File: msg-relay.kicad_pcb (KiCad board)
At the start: 2 copper layers, 100 x 100 mm, 6 parts, among them J1 Screw_Terminal_01x02, K1 SANYOU_SRD_Form_C, K2 SANYOU_SRD_Form_C, K3 SANYOU_SRD_Form_C, K4 SANYOU_SRD_Form_C

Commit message: Some work on schema
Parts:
- added D1: 1N4007, Diode_THT:D_DO-41_SOD81_P10.16mm_Horizontal, F.Cu at (146.9, 55.5)
- added D2: 1N4007, Diode_THT:D_DO-41_SOD81_P10.16mm_Horizontal, F.Cu at (147.4, 81.2)
- added D3: 1N4007, Diode_THT:D_DO-41_SOD81_P10.16mm_Horizontal, F.Cu at (144.6, 100.5)
- added D4: 1N4007, Diode_THT:D_DO-41_SOD81_P10.16mm_Horizontal, F.Cu at (149.1, 121.7)
- added J2: Conn_01x03_Male, Connector_Phoenix_MC_HighVoltage:PhoenixContact_MCV_1,5_3-G-5.08_1x03_P5.08mm_Vertical, F.Cu at (175.1, 55.7)
- added J3: Conn_01x03_Male, Connector_Phoenix_MC_HighVoltage:PhoenixContact_MCV_1,5_3-G-5.08_1x03_P5.08mm_Vertical, F.Cu at (175.5, 81.8)
- added J4: Conn_01x03_Male, Connector_Phoenix_MC_HighVoltage:PhoenixContact_MCV_1,5_3-G-5.08_1x03_P5.08mm_Vertical, F.Cu at (174.6, 101.3)
- added J5: Conn_01x03_Male, Connector_Phoenix_MC_HighVoltage:PhoenixContact_MCV_1,5_3-G-5.08_1x03_P5.08mm_Vertical, F.Cu at (176.4, 122.6)
- added Q1: BC847, Package_TO_SOT_SMD:SOT-23, F.Cu at (141.7, 65.5)
- added Q2: BC847, Package_TO_SOT_SMD:SOT-23, F.Cu at (141.8, 91.4)
- added Q3: BC847, Package_TO_SOT_SMD:SOT-23, F.Cu at (140.1, 110.7)
- added Q4: BC847, Package_TO_SOT_SMD:SOT-23, F.Cu at (144.3, 131.9)
- added R1: R, Resistor_SMD:R_0603_1608Metric, F.Cu at (142.2, 60.4)
- added R2: R, Resistor_SMD:R_0603_1608Metric, F.Cu at (142.7, 84.7)
- added R3: R, Resistor_SMD:R_0603_1608Metric, F.Cu at (141.2, 104.6)
- added R4: R, Resistor_SMD:R_0603_1608Metric, F.Cu at (143.4, 125.0)
- moved J1 81.2 mm to (115.2, 55.0)
- moved A1 36.5 mm to (125.7, 67.0), turned to 270 degrees
- moved K3 27.0 mm to (149.2, 106.3)
- moved K2 16.4 mm to (151.9, 87.0)
- moved K4 16.3 mm to (153.5, 127.6)
- moved K1 10.5 mm to (152.1, 61.1)
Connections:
- A1 pad 11: Net-(A1-Pad11) -> RELAY1
- A1 pad 12: Net-(A1-Pad12) -> RELAY2
- A1 pad 13: Net-(A1-Pad13) -> RELAY3
- A1 pad 14: Net-(A1-Pad14) -> RELAY4
- A1 pad 27: Net-(A1-Pad27) -> +5V
- A1 pad 29: Net-(A1-Pad29) -> GND
- A1 pad 30: Net-(A1-Pad30) -> +12V
- A1 pad 4: Net-(A1-Pad4) -> GND
- J1 pad 1: Net-(J1-Pad1) -> GND
- J1 pad 2: Net-(J1-Pad2) -> +12V
- K1 pad 5: Net-(K1-Pad5) -> +5V
- K2 pad 5: Net-(K2-Pad5) -> +5V
- K3 pad 5: Net-(K3-Pad5) -> +5V
- K4 pad 5: Net-(K4-Pad5) -> +5V
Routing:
- net Net-(J2-Pad2): track 0.00 -> 23.1 mm
- net Net-(D1-Pad2): track 0.00 -> 12.0 mm
- net Net-(J2-Pad3): track 0.00 -> 10.0 mm
- net Net-(J2-Pad1): track 0.00 -> 9.06 mm
- net +5V: track 0.00 -> 7.31 mm
- net Net-(Q1-Pad1): track 0.00 -> 4.00 mm

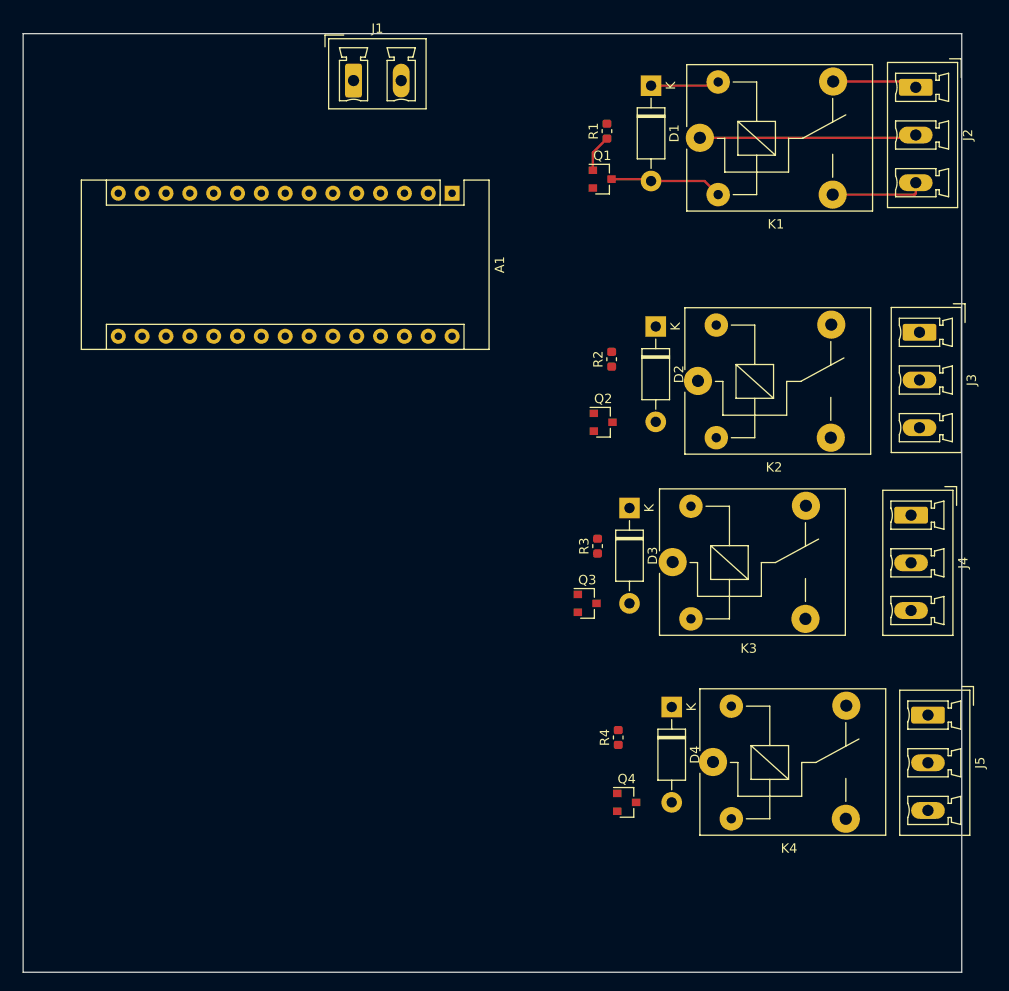
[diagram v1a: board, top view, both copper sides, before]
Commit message: Split out relay to own schema
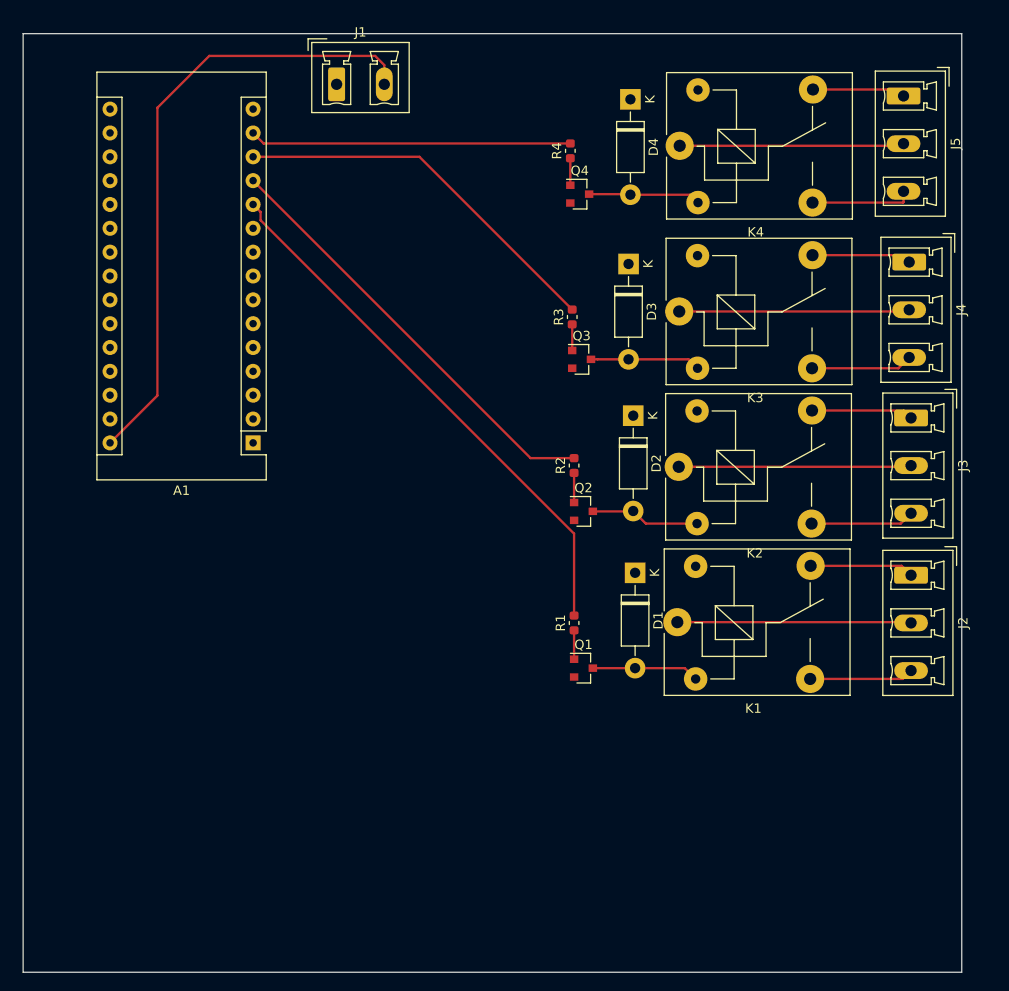
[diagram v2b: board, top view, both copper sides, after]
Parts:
- moved J5 66.0 mm to (173.8, 56.6)
- moved K4 65.7 mm to (149.9, 62.0)
- moved Q4 65.0 mm to (139.3, 67.1)
- moved D4 64.9 mm to (144.7, 57.0)
- moved R4 62.7 mm to (138.3, 62.5)
- moved R1 52.5 mm to (138.7, 112.8)
- moved Q1 52.1 mm to (139.7, 117.6)
- moved J2 52.0 mm to (174.6, 107.7)
- moved D1 51.9 mm to (145.2, 107.4)
- moved K1 51.7 mm to (149.7, 112.7)
- moved A1 34.0 mm to (104.5, 93.6), turned to 180 degrees
- moved J4 27.0 mm to (174.4, 74.3)
- moved K3 26.7 mm to (149.9, 79.6)
- moved Q3 26.0 mm to (139.5, 84.7)
- moved D3 26.0 mm to (144.5, 74.5)
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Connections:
- R2 pad 2: RELAY3 -> RELAY2
- R3 pad 2: RELAY4 -> RELAY3
- R4 pad 2: RELAY2 -> RELAY4
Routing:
- net +12V: track 0.00 -> 66.7 mm
- net RELAY1: track 0.00 -> 58.0 mm
- net RELAY2: track 0.00 -> 46.4 mm
- net RELAY3: track 0.00 -> 40.7 mm
- net RELAY4: track 0.00 -> 34.3 mm
- net Net-(J3-Pad2): track 0.00 -> 24.8 mm
- net Net-(J4-Pad2): track 0.00 -> 24.6 mm
- net Net-(J5-Pad2): track 0.00 -> 23.9 mm
- net Net-(D4-Pad2): track 0.00 -> 12.0 mm
- net Net-(D3-Pad2): track 0.00 -> 11.7 mm
- net Net-(D2-Pad2): track 0.00 -> 11.7 mm
- net Net-(J3-Pad3): track 0.00 -> 11.1 mm
- net Net-(J3-Pad1): track 0.00 -> 10.9 mm
- net Net-(J5-Pad3): track 0.00 -> 10.9 mm
- net Net-(J4-Pad3): track 0.00 -> 10.8 mm
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
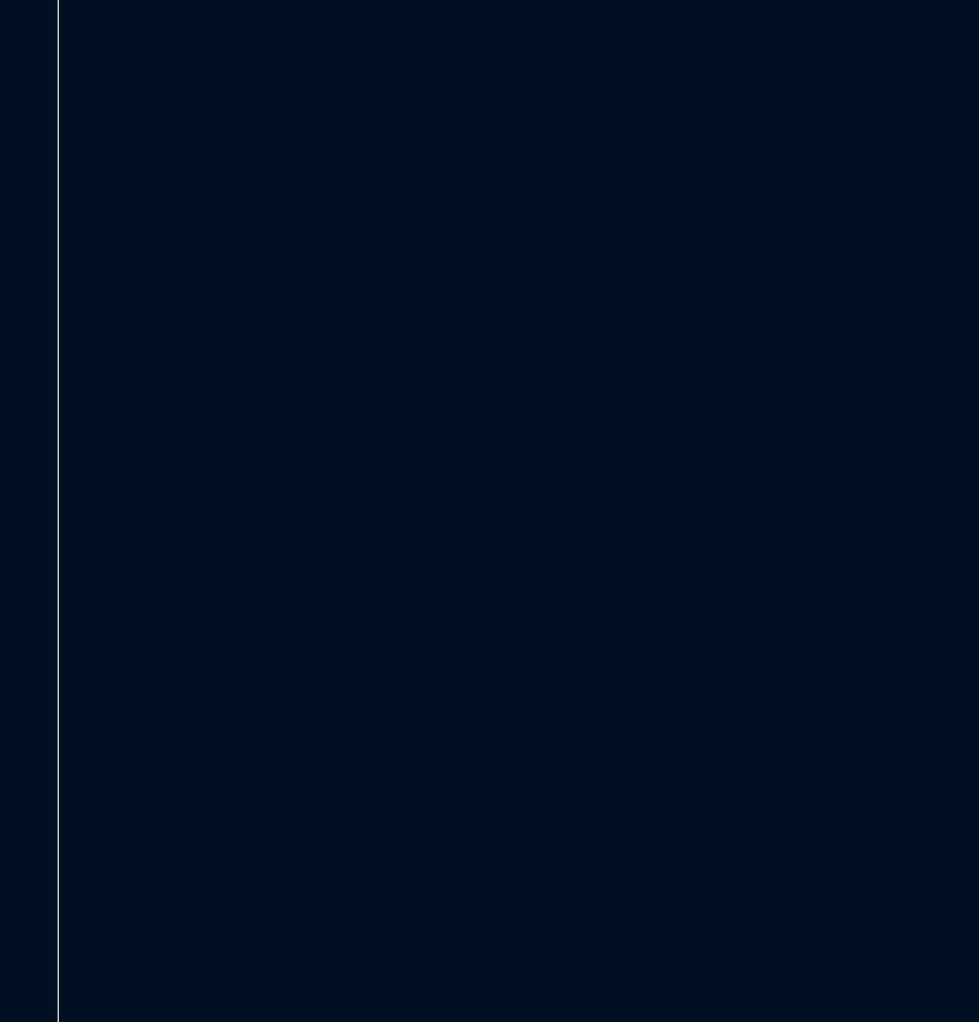
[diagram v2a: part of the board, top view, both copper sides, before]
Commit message: Added input module
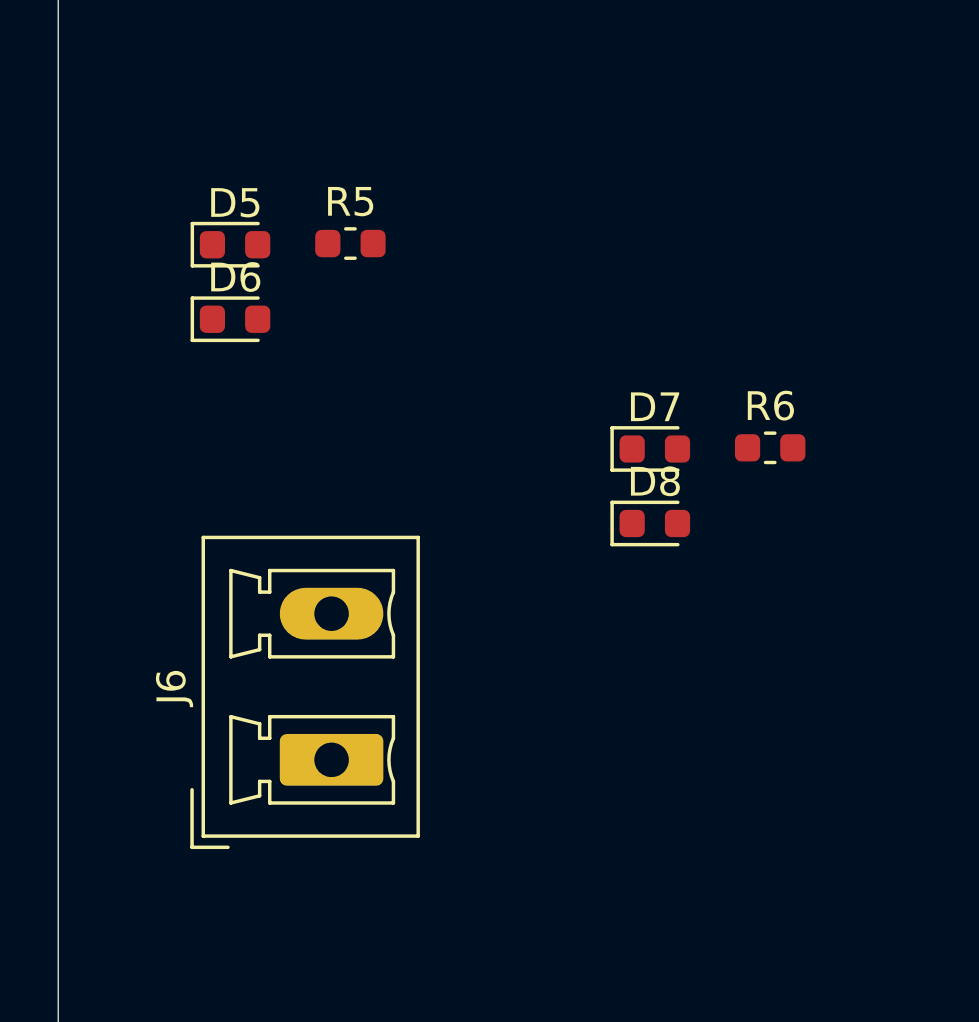
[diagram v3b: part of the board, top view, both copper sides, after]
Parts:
- added D5: D, Diode_SMD:D_0603_1608Metric, F.Cu at (86.1, 119.7)
- added D6: D, Diode_SMD:D_0603_1608Metric, F.Cu at (86.1, 122.3)
- added D7: D, Diode_SMD:D_0603_1608Metric, F.Cu at (100.7, 126.8)
- added D8: D, Diode_SMD:D_0603_1608Metric, F.Cu at (100.7, 129.4)
- added J6: Screw_Terminal_01x02, Connector_Phoenix_MC_HighVoltage:PhoenixContact_MCV_1,5_2-G-5.08_1x02_P5.08mm_Vertical, F.Cu at (89.5, 137.6)
- added R5: R, Resistor_SMD:R_0603_1608Metric, F.Cu at (90.2, 119.7)
- added R6: R, Resistor_SMD:R_0603_1608Metric, F.Cu at (104.7, 126.8)
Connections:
- A1 pad 5: Net-(A1-Pad5) -> /Input1/OUT
- A1 pad 6: Net-(A1-Pad6) -> /Input2/OUT

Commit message: Made v01
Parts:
- added D10: BAT43, Diode_THT:D_DO-35_SOD27_P7.62mm_Horizontal, F.Cu at (91.8, 123.0)
- added D11: BAT43, Diode_THT:D_DO-35_SOD27_P7.62mm_Horizontal, F.Cu at (101.2, 115.5)
- added D12: BAT43, Diode_THT:D_DO-35_SOD27_P7.62mm_Horizontal, F.Cu at (96.8, 123.0)
- added D9: BAT43, Diode_THT:D_DO-35_SOD27_P7.62mm_Horizontal, F.Cu at (87.2, 115.4)
- added J7: Conn_01x03_Male, Connector_Phoenix_MC_HighVoltage:PhoenixContact_MCV_1,5_3-G-5.08_1x03_P5.08mm_Vertical, F.Cu at (152.0, 111.0)
- added R10: 10k, Resistor_SMD:R_0603_1608Metric, F.Cu at (82.0, 122.2)
- added R11: 10k, Resistor_SMD:R_0603_1608Metric, F.Cu at (96.8, 127.2)
- added R12: 10k, Resistor_SMD:R_0603_1608Metric, F.Cu at (106.2, 122.3)
- added R7: 1k, Resistor_SMD:R_0603_1608Metric, F.Cu at (119.8, 111.0)
- added R8: 10k, Resistor_SMD:R_0603_1608Metric, F.Cu at (117.8, 122.0)
- added R9: 10k, Resistor_SMD:R_0603_1608Metric, F.Cu at (91.8, 127.5)
- D1, D3: value 1N4007 -> LED; footprint Diode_THT:D_DO-41_SOD81_P10.16mm_Horizontal -> LED_SMD:LED_0603_1608Metric
- D2, D4: value 1N4007 -> 1N4148; footprint Diode_THT:D_DO-41_SOD81_P10.16mm_Horizontal -> Diode_THT:D_DO-35_SOD27_P7.62mm_Horizontal
- D5, D7: value D -> LED; footprint Diode_SMD:D_0603_1608Metric -> LED_SMD:LED_0603_1608Metric
- D6, D8: value D -> 1N4148; footprint Diode_SMD:D_0603_1608Metric -> Diode_THT:D_DO-35_SOD27_P7.62mm_Horizontal
- J2: value Conn_01x03_Male -> Screw_Terminal_01x02; footprint Connector_Phoenix_MC_HighVoltage:PhoenixContact_MCV_1,5_3-G-5.08_1x03_P5.08mm_Vertical -> Connector_Phoenix_MC_HighVoltage:PhoenixContact_MCV_1,5_2-G-5.08_1x02_P5.08mm_Vertical
- J3: value Conn_01x03_Male -> Conn_01x04; footprint Connector_Phoenix_MC_HighVoltage:PhoenixContact_MCV_1,5_3-G-5.08_1x03_P5.08mm_Vertical -> Connector_PinSocket_1.27mm:PinSocket_1x04_P1.27mm_Vertical
- J6: value Screw_Terminal_01x02 -> Conn_01x03_Male; footprint Connector_Phoenix_MC_HighVoltage:PhoenixContact_MCV_1,5_2-G-5.08_1x02_P5.08mm_Vertical -> Connector_Phoenix_MC_HighVoltage:PhoenixContact_MCV_1,5_3-G-5.08_1x03_P5.08mm_Vertical
- R1, R3, R5: value R -> 1k
- R2, R4, R6: value R -> 10k
- moved J2 82.2 mm to (96.8, 134.0), turned to 180 degrees
- moved J6 77.4 mm to (152.0, 92.0), turned to 270 degrees
- moved J3 72.2 mm to (112.0, 55.0)
- moved R1 61.8 mm to (119.8, 54.0), turned to 180 degrees
- moved K4 59.0 mm to (128.8, 117.0)
- moved Q4 58.2 mm to (123.0, 123.0)
- moved K1 56.7 mm to (128.8, 60.0)
- moved D1 55.7 mm to (119.0, 58.3), turned to 90 degrees
- moved Q1 54.2 mm to (123.0, 66.0)
- moved D6 48.5 mm to (124.0, 92.0), turned to 270 degrees
- moved D2 42.3 mm to (124.0, 54.0)
- moved R5 40.5 mm to (119.8, 92.0), turned to 180 degrees
- moved D5 40.1 mm to (119.0, 96.8), turned to 90 degrees
- moved R2 37.2 mm to (118.2, 65.0), turned to 180 degrees
- moved A1 30.9 mm to (86.8, 68.3), turned to 0 degrees
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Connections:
- A1 pad 23: Net-(A1-Pad23) -> SDA
- A1 pad 24: Net-(A1-Pad24) -> SCL
- D1 pad 1: +5V -> Net-(D1-Pad1)
- D2 pad 2: Net-(D2-Pad2) -> Net-(D1-Pad1)
- D3 pad 1: +5V -> Net-(D3-Pad1)
- D4 pad 2: Net-(D4-Pad2) -> Net-(D3-Pad1)
- D5 pad 1: +5V -> Net-(D5-Pad1)
- D5 pad 2: /Input1/OUT -> Net-(D5-Pad2)
- D6 pad 1: /Input1/OUT -> +5V
- D6 pad 2: GND -> Net-(D5-Pad1)
- D7 pad 1: +5V -> Net-(D7-Pad1)
- D7 pad 2: /Input2/OUT -> Net-(D7-Pad2)
- D8 pad 1: /Input2/OUT -> +5V
- D8 pad 2: GND -> Net-(D7-Pad1)
- J2 pad 1: Net-(J2-Pad1) -> INPUT2
- J2 pad 2: Net-(J2-Pad2) -> INPUT1
- J3 pad 1: Net-(J3-Pad1) -> SDA
- J3 pad 2: Net-(J3-Pad2) -> SCL
- J3 pad 3: Net-(J3-Pad3) -> +5V
- J6 pad 1: INPUT2 -> Net-(J6-Pad1)
- J6 pad 2: INPUT1 -> Net-(J6-Pad2)
- K1 pad 1: Net-(J2-Pad2) -> Net-(J4-Pad2)
- K1 pad 2: Net-(D1-Pad2) -> Net-(D1-Pad1)
- K1 pad 3: Net-(J2-Pad3) -> Net-(J4-Pad3)
- K1 pad 4: Net-(J2-Pad1) -> Net-(J4-Pad1)
- K2 pad 1: Net-(J3-Pad2) -> Net-(J5-Pad2)
- K2 pad 2: Net-(D2-Pad2) -> Net-(D3-Pad1)
- K2 pad 3: Net-(J3-Pad3) -> Net-(J5-Pad3)
- K2 pad 4: Net-(J3-Pad1) -> Net-(J5-Pad1)
- K3 pad 1: Net-(J4-Pad2) -> Net-(J6-Pad2)
- K3 pad 2: Net-(D3-Pad2) -> Net-(D5-Pad1)
- K3 pad 3: Net-(J4-Pad3) -> Net-(J6-Pad3)
- K3 pad 4: Net-(J4-Pad1) -> Net-(J6-Pad1)
- K4 pad 1: Net-(J5-Pad2) -> Net-(J7-Pad2)
- K4 pad 2: Net-(D4-Pad2) -> Net-(D7-Pad1)
- K4 pad 3: Net-(J5-Pad3) -> Net-(J7-Pad3)
- K4 pad 4: Net-(J5-Pad1) -> Net-(J7-Pad1)
- Q1 pad 3: Net-(D1-Pad2) -> Net-(D1-Pad1)
- Q2 pad 3: Net-(D2-Pad2) -> Net-(D3-Pad1)
- Q3 pad 3: Net-(D3-Pad2) -> Net-(D5-Pad1)
- Q4 pad 3: Net-(D4-Pad2) -> Net-(D7-Pad1)
- R1 pad 1: Net-(Q1-Pad1) -> +5V
- R1 pad 2: RELAY1 -> Net-(D1-Pad2)
- R2 pad 1: Net-(Q2-Pad1) -> Net-(Q1-Pad1)
- R2 pad 2: RELAY2 -> RELAY1
- R3 pad 1: Net-(Q3-Pad1) -> +5V
- R3 pad 2: RELAY3 -> Net-(D3-Pad2)
- R4 pad 1: Net-(Q4-Pad1) -> Net-(Q2-Pad1)
- R4 pad 2: RELAY4 -> RELAY2
- R5 pad 1: /Input1/OUT -> +5V
- R5 pad 2: INPUT1 -> Net-(D5-Pad2)
- R6 pad 1: /Input2/OUT -> Net-(Q3-Pad1)
- R6 pad 2: INPUT2 -> RELAY3
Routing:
- net /Input2/OUT: track 0.00 -> 66.1 mm
- net /Input1/OUT: track 0.00 -> 65.4 mm
- net +12V: track 66.7 -> 18.9 mm
- net SDA: track 0.00 -> 35.2 mm
- net SCL: track 0.00 -> 32.2 mm
- net Net-(J2-Pad2): track 24.9 -> 0.00 mm
- net Net-(J3-Pad2): track 24.8 -> 0.00 mm
- net Net-(J7-Pad2): track 0.00 -> 23.6 mm
- net Net-(J6-Pad2): track 0.00 -> 23.6 mm
- net RELAY1: track 58.0 -> 77.5 mm
- net Net-(D3-Pad1): track 0.00 -> 17.9 mm
- net Net-(D1-Pad1): track 0.00 -> 17.6 mm
- net Net-(D5-Pad1): track 0.00 -> 17.5 mm
- net Net-(D7-Pad1): track 0.00 -> 17.4 mm
- net RELAY2: track 46.4 -> 61.0 mm
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- added copper zone on B.Cu, net +5V
- added copper zone on F.Cu, net GND
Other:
- board size 100 x 100 mm -> 77 x 90.2 mm
- net class Default: trace_width 0.25 -> 0.5
- net class Power added: clearance 0.2, trace_width 1, via_dia 0.8, via_drill 0.4
- rule pad_to_mask_clearance: 0.051 -> 0.05
- rule solder_mask_min_width: 0.25 -> 0.3
- rule trace_min: 0.2 -> 0.5
- rule via_min_drill: 0.3 -> 0.4
- rule via_min_size: 0.4 -> 0.8
- board text added: "MSG-Relay v01"
- board text added: "v01"
